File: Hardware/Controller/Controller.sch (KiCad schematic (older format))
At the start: 60 parts, among them J1 8P8C, J2 LCD Header, J3 USB_B_Micro, J4 S88 ShiftRegister, J5 Screw_Terminal_01x05, SW1 Rotary_Encoder_Switch, SW2 SW_F0, SW3 SW_F1, SW4 SW_F2, SW5 SW_F3, SW6 SW_F4, SW7 Shift, SW8 Stop, U1 ESP32-WROOM-32, U2 TJA1051T, U3 74LS367, U4 CH340C, U5 XM1584

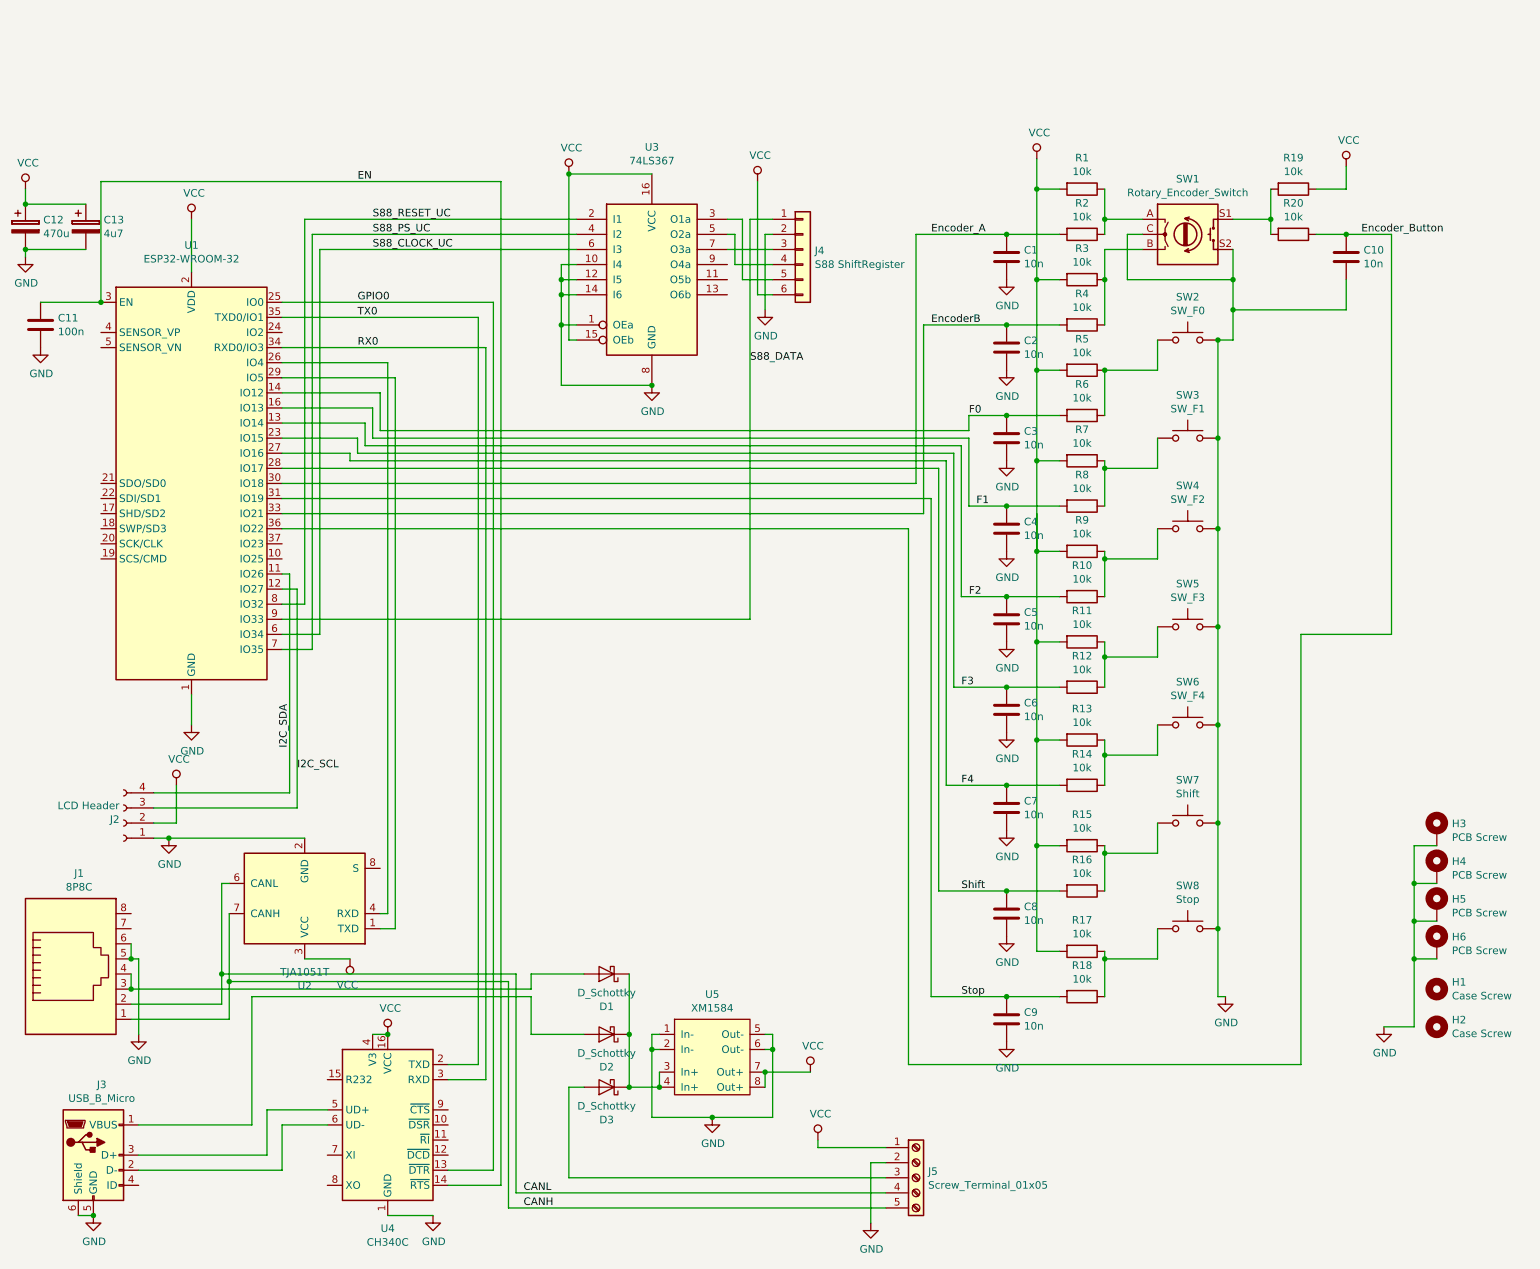
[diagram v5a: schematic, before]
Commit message: Finished PCB
* Reordered some pins to make the PCB layout easier
* Added connector descriptions
* Adjusted Silkscreen Items
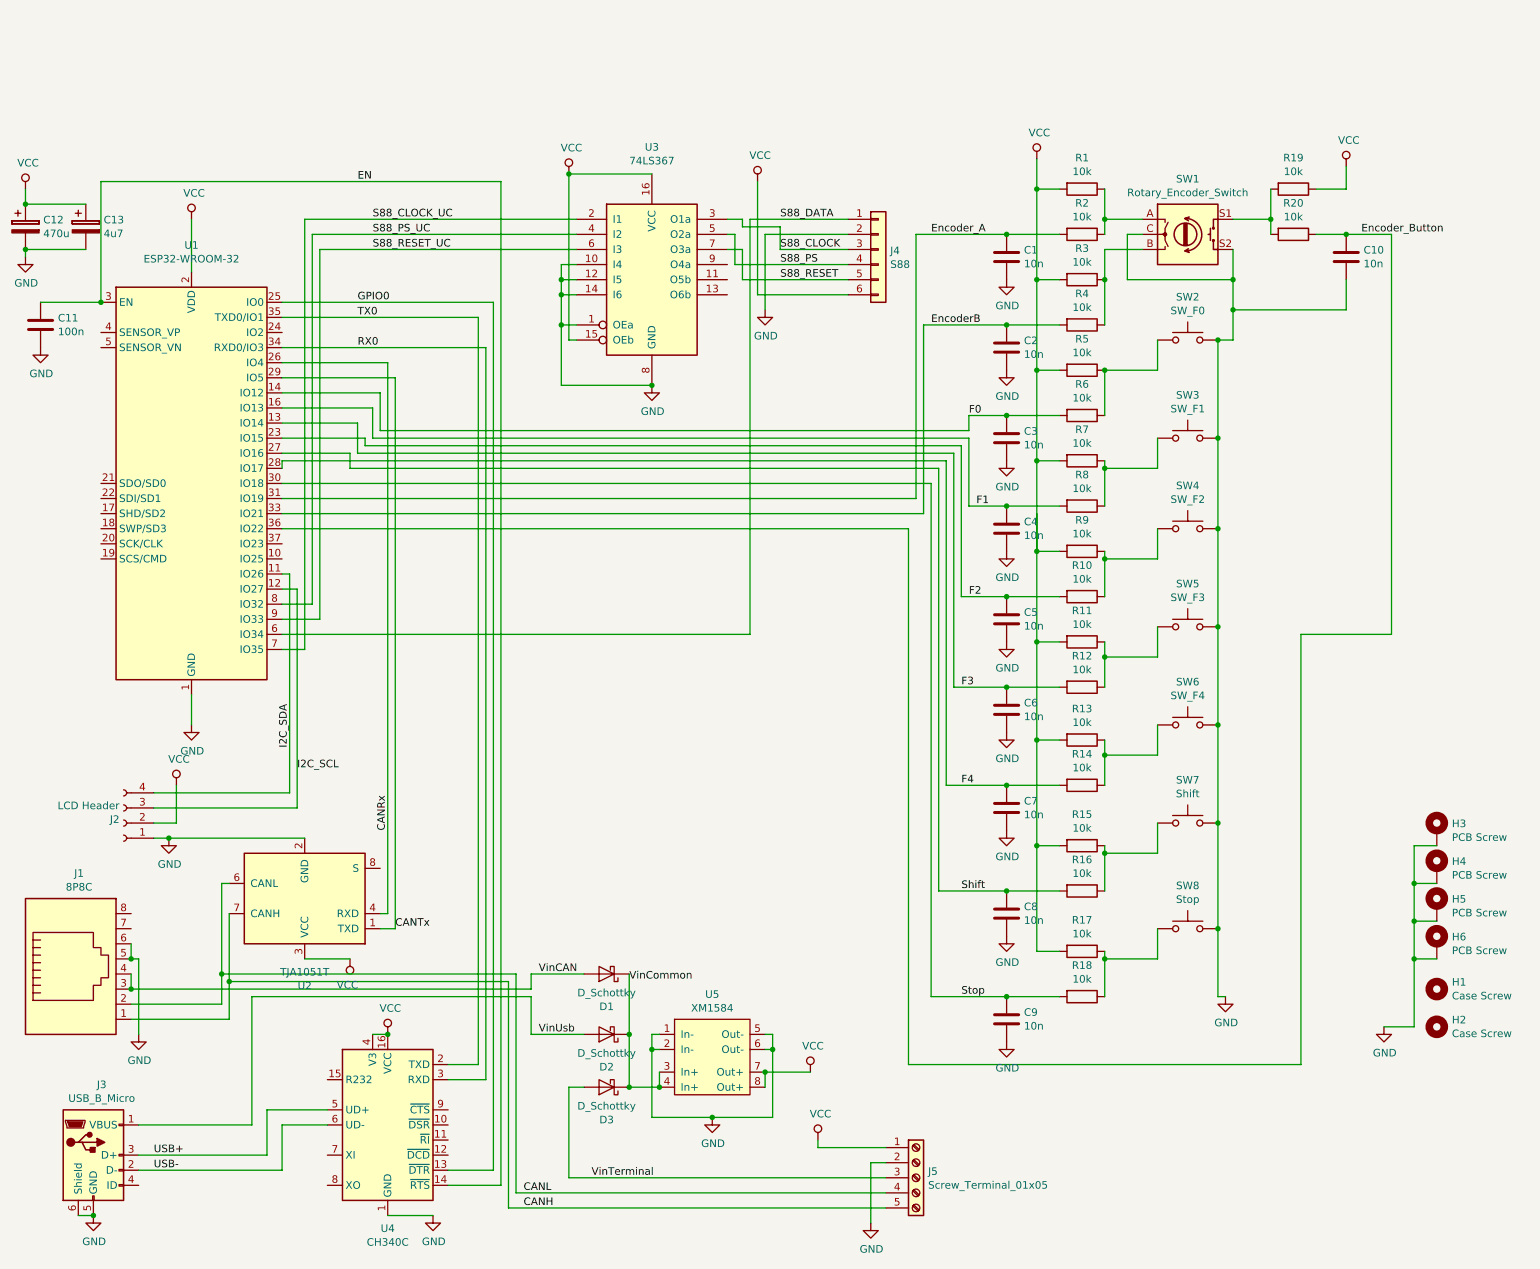
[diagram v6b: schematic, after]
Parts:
- C12: footprint Capacitor_THT:CP_Radial_D6.3mm_P2.50mm -> Capacitor_SMD:CP_Elec_6.3x7.7
- C13: footprint Capacitor_THT:CP_Radial_D6.3mm_P2.50mm -> Capacitor_Tantalum_SMD:CP_EIA-3216-18_Kemet-A_Pad1.58x1.35mm_HandSolder
- H3, H4, H5, H6: footprint MountingHole:MountingHole_2.7mm_M2.5 -> MountingHole:MountingHole_2.7mm_M2.5_Pad_Via
- J4: value S88 ShiftRegister -> S88
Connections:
- net Encoder_A: now also U1.31 (IO19); no longer U1.30 (IO18)
- net F2: now also U1.23 (IO15); no longer U1.13 (IO14)
- net F3: now also U1.13 (IO14); no longer U1.23 (IO15)
- net F4: now also U1.28 (IO17); no longer U1.27 (IO16)
- net S88_CLOCK_UC: now also U1.7 (IO35), U3.2 (I1); no longer U1.6 (IO34), U3.6 (I3)
- net S88_DATA: now also U1.6 (IO34); no longer U1.9 (IO33)
- net S88_PS_UC: now also U1.8 (IO32); no longer U1.7 (IO35)
- net S88_RESET_UC: now also U1.9 (IO33), U3.6 (I3); no longer U1.8 (IO32), U3.2 (I1)
- net Shift: now also U1.27 (IO16); no longer U1.28 (IO17)
- net Stop: now also U1.30 (IO18); no longer U1.31 (IO19)
- net CANRx: now reaches U1.26 (IO4), U2.4 (RXD)
- net CANTx: now reaches U1.29 (IO5), U2.1 (TXD)
- net VinCAN: now reaches D1.2 (A), J1.3, J1.4
- net VinUsb: now reaches D2.2 (A), J3.1 (VBUS)
- net USB-: now reaches J3.2 (D-), U4.6 (UD-)
- net USB+: now reaches J3.3 (D+), U4.5 (UD+)
- net S88_CLOCK: now reaches J4.3 (Pin_3)
- net S88_CLOCK: now also U3.3 (O1a); no longer U3.7 (O3a)
- net S88_PS: now reaches J4.4 (Pin_4), U3.5 (O2a)
- net S88_RESET: now reaches J4.5 (Pin_5)
- net S88_RESET: now also U3.7 (O3a); no longer U3.3 (O1a)
- net VinTerminal: now reaches D3.2 (A), J5.3 (Pin_3)
- net VinCommon: now reaches D1.1 (K), D2.1 (K), D3.1 (K), U5.3 (In+), U5.4 (In+)
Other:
- moved on the sheet: J4
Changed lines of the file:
@@
 F 0 "H6" H 10100 5796 50  0000 L CNN
 F 1 "PCB Screw" H 10100 5705 50  0000 L CNN
-F 2 "MountingHole:MountingHole_2.7mm_M2.5" H 10000 5750 50  0001 C CNN
+F 2 "MountingHole:MountingHole_2.7mm_M2.5_Pad_Via" H 10000 5750 50  0001 C CNN
 F 3 "~" H 10000 5750 50  0001 C CNN
 	1    10000 5750
@@
 F 0 "H5" H 10100 5546 50  0000 L CNN
 F 1 "PCB Screw" H 10100 5455 50  0000 L CNN
-F 2 "MountingHole:MountingHole_2.7mm_M2.5" H 10000 5500 50  0001 C CNN
+F 2 "MountingHole:MountingHole_2.7mm_M2.5_Pad_Via" H 10000 5500 50  0001 C CNN
 F 3 "~" H 10000 5500 50  0001 C CNN
 	1    10000 5500
@@
 F 0 "H4" H 10100 5296 50  0000 L CNN
 F 1 "PCB Screw" H 10100 5205 50  0000 L CNN
-F 2 "MountingHole:MountingHole_2.7mm_M2.5" H 10000 5250 50  0001 C CNN
+F 2 "MountingHole:MountingHole_2.7mm_M2.5_Pad_Via" H 10000 5250 50  0001 C CNN
 F 3 "~" H 10000 5250 50  0001 C CNN
 	1    10000 5250
@@
 F 0 "H3" H 10100 5046 50  0000 L CNN
 F 1 "PCB Screw" H 10100 4955 50  0000 L CNN
-F 2 "MountingHole:MountingHole_2.7mm_M2.5" H 10000 5000 50  0001 C CNN
+F 2 "MountingHole:MountingHole_2.7mm_M2.5_Pad_Via" H 10000 5000 50  0001 C CNN
 F 3 "~" H 10000 5000 50  0001 C CNN
 	1    10000 5000
@@
 L Connector_Generic:Conn_01x06 J4
 U 1 1 5C69531D
-P 5800 1150
-F 0 "J4" H 5879 1142 50  0000 L CNN
-F 1 "S88 ShiftRegister" H 5879 1051 50  0000 L CNN
-F 2 "Connector_Molex:Molex_Micro-Latch_53254-0670_1x06_P2.00mm_Horizontal" H 5800 1150 50  0001 C CNN
-F 3 "~" H 5800 1150 50  0001 C CNN
-	1    5800 1150
+P 6300 1150
+F 0 "J4" H 6379 1142 50  0000 L CNN
+F 1 "S88" H 6379 1051 50  0000 L CNN
+F 2 "Connector_Molex:Molex_Micro-Latch_53254-0670_1x06_P2.00mm_Horizontal" H 6300 1150 50  0001 C CNN
+F 3 "~" H 6300 1150 50  0001 C CNN
+	1    6300 1150
 	1    0    0    -1
 $EndComp
@@
 	5500 700  5500 1450
 Wire Wire Line
-	5500 1450 5600 1450
+	5500 1450 6100 1450
 $Comp
 L power:GND #PWR0125
@@
 $EndComp
 Wire Wire Line
-	5600 1050 5550 1050
+	6100 1050 5550 1050
 Wire Wire Line
 	5550 1050 5550 1550
-Text Label 2950 950  0    50   ~ 0
+Text Label 2950 1150 0    50   ~ 0
 S88_RESET_UC
 Text Label 2950 1050 0    50   ~ 0
 S88_PS_UC
-Text Label 2950 1150 0    50   ~ 0
+Text Label 2950 950  0    50   ~ 0
 S88_CLOCK_UC
 Wire Wire Line
-	5450 950  5600 950
-Text Label 5450 1900 0    50   ~ 0
+	5450 950  6100 950
+Text Label 5650 950  0    50   ~ 0
 S88_DATA
 Wire Wire Line
-	5600 1350 5400 1350
-Wire Wire Line
-	5400 1350 5400 950
-Wire Wire Line
-	5400 950  5300 950
-Wire Wire Line
-	5600 1150 5300 1150
+	6100 1350 5400 1350
+Wire Wire Line
+	5400 1350 5400 1150
 Wire Wire Line
 	5300 1050 5350 1050
@@
 	5350 1050 5350 1250
 Wire Wire Line
-	5350 1250 5600 1250
-Wire Wire Line
-	6550 2700 6550 1050
+	5350 1250 6100 1250
+Wire Wire Line
+	6550 2800 6550 1050
 Wire Wire Line
 	6550 1050 7150 1050
@@
 Connection ~ 9400 1050
 Wire Wire Line
-	2350 2100 3000 2100
-Wire Wire Line
-	3000 2100 3000 2350
-Wire Wire Line
 	3000 2350 6900 2350
 Wire Wire Line
@@
 Connection ~ 7150 2250
 Wire Wire Line
-	2350 2200 2950 2200
-Wire Wire Line
-	2950 2200 2950 2400
-Wire Wire Line
 	2950 2400 6900 2400
 Wire Wire Line
@@
 Connection ~ 7150 2850
 Wire Wire Line
-	2350 2300 2900 2300
-Wire Wire Line
-	2900 2300 2900 2450
-Wire Wire Line
 	2900 2450 6850 2450
 Wire Wire Line
@@
 Connection ~ 7150 3450
 Wire Wire Line
-	2350 2400 2850 2400
-Wire Wire Line
-	2850 2400 2850 2500
-Wire Wire Line
 	2850 2500 6800 2500
 Wire Wire Line
@@
 Connection ~ 7150 4050
 Wire Wire Line
-	2350 2500 2800 2500
-Wire Wire Line
-	2800 2500 2800 2550
-Wire Wire Line
-	2800 2550 6750 2550
-Wire Wire Line
 	6750 2550 6750 4700
 Wire Wire Line
@@
 Connection ~ 7150 4700
 Wire Wire Line
-	2350 2600 6700 2600
-Wire Wire Line
 	6700 2600 6700 5400
 Wire Wire Line
@@
 Connection ~ 7150 5400
 Wire Wire Line
-	2350 2800 6650 2800
-Wire Wire Line
-	6650 2800 6650 6100
+	6650 2700 6650 6100
 Wire Wire Line
 	6650 6100 7150 6100
@@
 	4300 950  2500 950
 Wire Wire Line
-	5450 950  5450 3600
-Wire Wire Line
-	5450 3600 2350 3600
-Wire Wire Line
-	2600 1150 2600 3700
-Wire Wire Line
-	2600 3700 2350 3700
-Wire Wire Line
-	2550 1050 2550 3800
-Wire Wire Line
-	2550 3800 2350 3800
-Wire Wire Line
-	2500 950  2500 3500
-Wire Wire Line
-	2500 3500 2350 3500
+	5450 950  5450 3700
+Wire Wire Line
+	2600 1150 2600 3600
+Wire Wire Line
+	2550 1050 2550 3500
+Wire Wire Line
+	2500 950  2500 3800
 $Comp
 L Device:C C11
@@
 	750  1500 1150 1500
 Connection ~ 1150 1500
-Wire Wire Line
-	6550 2700 2350 2700
 Wire Wire Line
 	6600 2900 2350 2900
@@
 F 0 "C12" H 768 1046 50  0000 L CNN
 F 1 "470u" H 768 955 50  0000 L CNN
-F 2 "Capacitor_THT:CP_Radial_D6.3mm_P2.50mm" H 688 850 50  0001 C CNN
+F 2 "Capacitor_SMD:CP_Elec_6.3x7.7" H 688 850 50  0001 C CNN
 F 3 "~" H 650 1000 50  0001 C CNN
 	1    650  1000
@@
 F 0 "C13" H 1168 1046 50  0000 L CNN
 F 1 "4u7" H 1168 955 50  0000 L CNN
-F 2 "Capacitor_THT:CP_Radial_D6.3mm_P2.50mm" H 1088 850 50  0001 C CNN
+F 2 "Capacitor_Tantalum_SMD:CP_EIA-3216-18_Kemet-A_Pad1.58x1.35mm_HandSolder" H 1088 850 50  0001 C CNN
 F 3 "~" H 1050 1000 50  0001 C CNN
 	1    1050 1000
@@
 Text Label 2850 700  0    50   ~ 0
 EN
+Text Label 4650 6000 0    50   ~ 0
+VinCommon
+Text Label 4400 7300 0    50   ~ 0
+VinTerminal
+Text Label 4050 6350 0    50   ~ 0
+VinUsb
+Text Label 4050 5950 0    50   ~ 0
+VinCAN
+Text Label 1500 7150 0    50   ~ 0
+USB+
+Text Label 1500 7250 0    50   ~ 0
+USB-
+Wire Wire Line
+	5450 3700 2350 3700
+Wire Wire Line
+	2550 3500 2350 3500
+Text Label 3100 5650 0    50   ~ 0
+CANTx
+Text Label 3050 5000 1    50   ~ 0
+CANRx
+Wire Wire Line
+	3000 2350 3000 2100
+Wire Wire Line
+	3000 2100 2350 2100
+Wire Wire Line
+	2850 2500 2850 2300
+Wire Wire Line
+	2850 2300 2350 2300
+Wire Wire Line
+	2950 2400 2950 2200
+Wire Wire Line
+	2950 2200 2350 2200
+Wire Wire Line
+	2900 2450 2900 2400
+Wire Wire Line
+	2900 2400 2350 2400
+Wire Wire Line
+	6650 2700 2350 2700
+Wire Wire Line
+	6550 2800 2350 2800
+Wire Wire Line
+	2350 2550 2350 2600
+Wire Wire Line
+	2350 2550 6750 2550
+Wire Wire Line
+	2350 2500 2800 2500
+Wire Wire Line
+	2800 2500 2800 2600
+Wire Wire Line
+	2800 2600 6700 2600
+Wire Wire Line
+	2600 3600 2350 3600
+Wire Wire Line
+	2500 3800 2350 3800
+Text Label 5650 1150 0    50   ~ 0
+S88_CLOCK
+Text Label 5650 1250 0    50   ~ 0
+S88_PS
+Text Label 5650 1350 0    50   ~ 0
+S88_RESET
+Wire Wire Line
+	5300 1150 5400 1150
+Wire Wire Line
+	5300 950  5400 950
+Wire Wire Line
+	5400 950  5400 1000
+Wire Wire Line
+	5400 1000 5650 1000
+Wire Wire Line
+	5650 1000 5650 1150
+Wire Wire Line
+	6100 1150 5650 1150
 $EndSCHEMATC

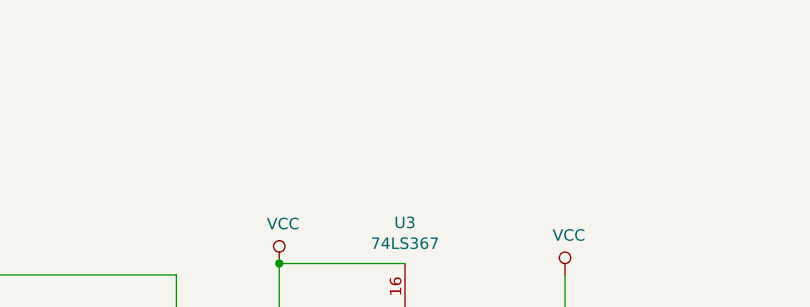
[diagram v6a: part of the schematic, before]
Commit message: Updated USB Port
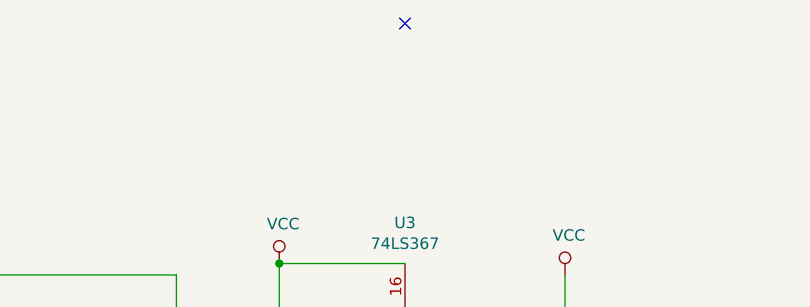
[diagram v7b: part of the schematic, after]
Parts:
- J3: footprint Connector_USB:USB_Micro-B_Amphenol_10103594-0001LF_Horizontal -> Connector_USB:USB_Micro-B_Molex_47346-0001
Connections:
- no-connect marks 0 -> 1
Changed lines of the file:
@@
 F 0 "J3" H 1155 7617 50  0000 C CNN
 F 1 "USB_B_Micro" H 1155 7526 50  0000 C CNN
-F 2 "Connector_USB:USB_Micro-B_Amphenol_10103594-0001LF_Horizontal" H 1250 7100 50  0001 C CNN
+F 2 "Connector_USB:USB_Micro-B_Molex_47346-0001" H 1250 7100 50  0001 C CNN
 F 3 "~" H 1250 7100 50  0001 C CNN
 	1    1100 7150
@@
 Wire Wire Line
 	6100 1150 5650 1150
+NoConn ~ 4800 -400
 $EndSCHEMATC

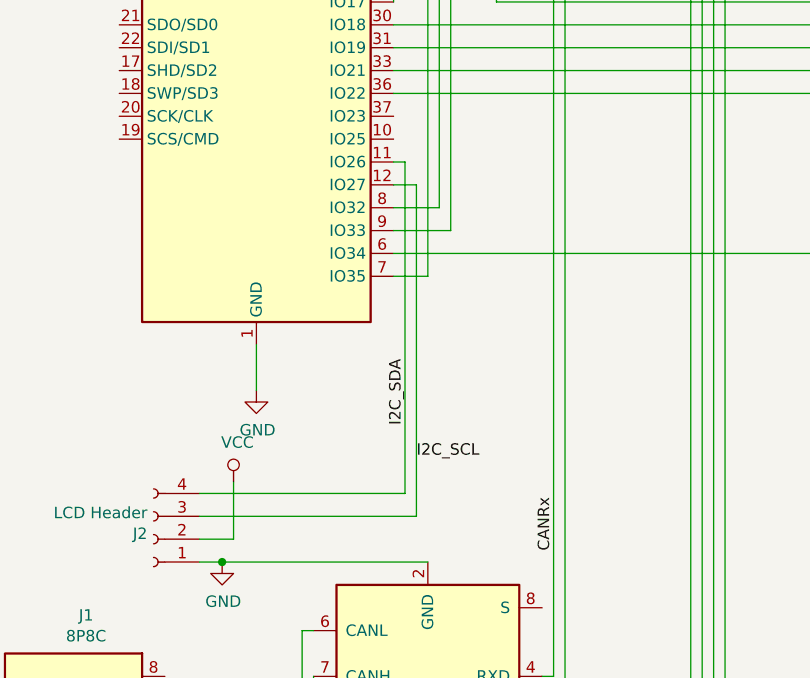
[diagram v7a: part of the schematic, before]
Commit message: Optimizations
* Moved Screen connector to the other side
* Optimized knee bends
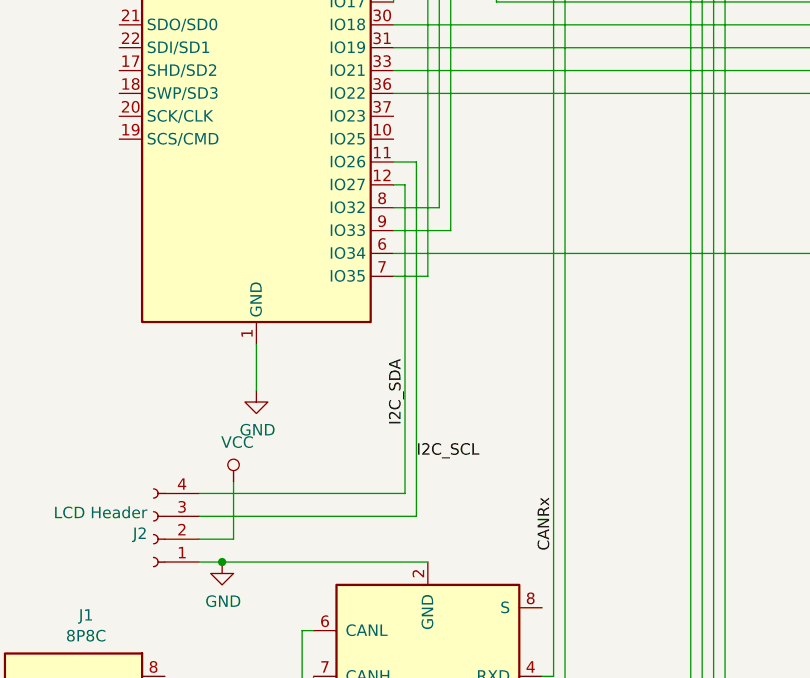
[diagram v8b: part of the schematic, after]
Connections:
- net I2C_SCL: now also U1.11 (IO26); no longer U1.12 (IO27)
- net I2C_SDA: now also U1.12 (IO27); no longer U1.11 (IO26)
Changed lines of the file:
@@
 	9850 5350 9850 5600
-$Comp
-L RF_Module:ESP32-WROOM-32 U1
-U 1 1 5C688B86
-P 1750 2700
-F 0 "U1" H 1750 4278 50  0000 C CNN
-F 1 "ESP32-WROOM-32" H 1750 4187 50  0000 C CNN
-F 2 "RF_Module:ESP32-WROOM-32" H 1750 1200 50  0001 C CNN
-F 3 "https://www.espressif.com/sites/default/files/documentation/esp32-wroom-32d_esp32-wroom-32u_datasheet_en.pdf" H 1450 2750 50  0001 C CNN
-	1    1750 2700
-	1    0    0    -1
-$EndComp
 $Comp
 L Connector:8P8C J1
@@
 $EndComp
 Wire Wire Line
-	2400 3300 2400 4750
+	2400 3400 2400 4750
 Wire Wire Line
 	2400 4750 1500 4750
 Wire Wire Line
-	2450 3400 2450 4850
+	2450 3300 2450 4850
 Wire Wire Line
 	2450 4850 1500 4850
@@
 Wire Wire Line
 	750  1500 1150 1500
-Connection ~ 1150 1500
 Wire Wire Line
 	6600 2900 2350 2900
@@
 Wire Wire Line
 	9850 5850 9850 6300
-Wire Wire Line
-	2450 3400 2350 3400
-Wire Wire Line
-	2400 3300 2350 3300
 Text Label 6900 2250 0    50   ~ 0
 F0
@@
 	6100 1150 5650 1150
 NoConn ~ 4800 -400
+Connection ~ 1150 1500
+$Comp
+L RF_Module:ESP32-WROOM-32 U1
+U 1 1 5C688B86
+P 1750 2700
+F 0 "U1" H 1750 4278 50  0000 C CNN
+F 1 "ESP32-WROOM-32" H 1750 4187 50  0000 C CNN
+F 2 "RF_Module:ESP32-WROOM-32" H 1750 1200 50  0001 C CNN
+F 3 "https://www.espressif.com/sites/default/files/documentation/esp32-wroom-32d_esp32-wroom-32u_datasheet_en.pdf" H 1450 2750 50  0001 C CNN
+	1    1750 2700
+	1    0    0    -1
+$EndComp
+Wire Wire Line
+	2400 3400 2350 3400
+Wire Wire Line
+	2450 3300 2350 3300
 $EndSCHEMATC
